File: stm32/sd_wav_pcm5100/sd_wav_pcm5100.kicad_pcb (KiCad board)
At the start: 2 copper layers, 39.7 x 50 mm, 79 parts, among them J1 BTN_1-4, J2 BTN_5-7, J3 BTN_8-11, P1 ST-LINK, P2 SPK_OUTL, P3 SPK_OUTR, P4 Supply, U1 STM32F410RBT6, U2 PCM5100, U3 PAM8403, U4 MX-503398-1892

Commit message: [sd_wav_pcm5100] updated board rev to 0.1
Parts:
- added REF**: 1pin, myfootprints:1pin, F.Cu at (72.8, 113.8)
- added REF**: 1pin, myfootprints:1pin, F.Cu at (73.8, 113.8)
- added REF**: 1pin, myfootprints:1pin, F.Cu at (72.8, 114.8)
- added REF**: 1pin, myfootprints:1pin, F.Cu at (73.8, 114.8)
- added REF**: 1pin, myfootprints:1pin, F.Cu at (73.8, 116.8)
- added REF**: 1pin, myfootprints:1pin, F.Cu at (72.8, 115.8)
- added REF**: 1pin, myfootprints:1pin, F.Cu at (73.8, 115.8)
- added REF**: 1pin, myfootprints:1pin, F.Cu at (72.8, 116.8)
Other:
- board text added: "Rev 0.1"
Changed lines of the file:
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@@
 (kicad_pcb (version 20160815) (host pcbnew no-vcs-found-7448~57~ubuntu16.04.1)
   (general
-    (links 146)
+    (links 154)
     (no_connects 0)
-    (area 56.39875 66.41875 100.59575 118.54175)
+    (area 59.074999 68.374999 98.875001 118.450018)
     (thickness 1.6)
-    (drawings 22)
-    (tracks 484)
+    (drawings 23)
+    (tracks 482)
     (zones 0)
-    (modules 79)
+    (modules 87)
     (nets 51)
   )
@@
     (add_net "Net-(R6-Pad2)")
   )
+  (module myfootprints:1pin (layer F.Cu)
+    (at 72.75 113.8)
+    (descr "module 1 pin (ou trou mecanique de percage)")
+    (tags DEV)
+    (fp_text reference REF** (at 0 -3.048) (layer F.SilkS) hide
+      (effects (font (size 0.6 0.6) (thickness 0.125)))
+    )
+    (fp_text value 1pin (at 0 2.794) (layer F.Fab) hide
+      (effects (font (size 0.6 0.6) (thickness 0.125)))
+    )
+    (pad "" thru_hole circle (at 0 0) (size 0.8 0.8) (drill 0.4) (layers *.Cu)
+      (net 1 GND) (zone_connect 2))
+  )
+  (module myfootprints:1pin (layer F.Cu)
+    (at 73.75 113.8)
+    (descr "module 1 pin (ou trou mecanique de percage)")
+    (tags DEV)
+    (fp_text reference REF** (at 0 -3.048) (layer F.SilkS) hide
+      (effects (font (size 0.6 0.6) (thickness 0.125)))
+    )
+    (fp_text value 1pin (at 0 2.794) (layer F.Fab) hide
+      (effects (font (size 0.6 0.6) (thickness 0.125)))
+    )
+    (pad "" thru_hole circle (at 0 0) (size 0.8 0.8) (drill 0.4) (layers *.Cu)
+      (net 1 GND) (zone_connect 2))
+  )
+  (module myfootprints:1pin (layer F.Cu)
+    (at 72.75 114.8)
+    (descr "module 1 pin (ou trou mecanique de percage)")
+    (tags DEV)
+    (fp_text reference REF** (at 0 -3.048) (layer F.SilkS) hide
+      (effects (font (size 0.6 0.6) (thickness 0.125)))
+    )
+    (fp_text value 1pin (at 0 2.794) (layer F.Fab) hide
+      (effects (font (size 0.6 0.6) (thickness 0.125)))
+    )
+    (pad "" thru_hole circle (at 0 0) (size 0.8 0.8) (drill 0.4) (layers *.Cu)
+      (net 1 GND) (zone_connect 2))
+  )
+  (module myfootprints:1pin (layer F.Cu)
+    (at 73.75 114.8)
+    (descr "module 1 pin (ou trou mecanique de percage)")
+    (tags DEV)
+    (fp_text reference REF** (at 0 -3.048) (layer F.SilkS) hide
+      (effects (font (size 0.6 0.6) (thickness 0.125)))
+    )
+    (fp_text value 1pin (at 0 2.794) (layer F.Fab) hide
+      (effects (font (size 0.6 0.6) (thickness 0.125)))
+    )
+    (pad "" thru_hole circle (at 0 0) (size 0.8 0.8) (drill 0.4) (layers *.Cu)
+      (net 1 GND) (zone_connect 2))
+  )
+  (module myfootprints:1pin (layer F.Cu)
+    (at 73.75 116.8)
+    (descr "module 1 pin (ou trou mecanique de percage)")
+    (tags DEV)
+    (fp_text reference REF** (at 0 -3.048) (layer F.SilkS) hide
+      (effects (font (size 0.6 0.6) (thickness 0.125)))
+    )
+    (fp_text value 1pin (at 0 2.794) (layer F.Fab) hide
+      (effects (font (size 0.6 0.6) (thickness 0.125)))
+    )
+    (pad "" thru_hole circle (at 0 0) (size 0.8 0.8) (drill 0.4) (layers *.Cu)
+      (net 1 GND) (zone_connect 2))
+  )
+  (module myfootprints:1pin (layer F.Cu)
+    (at 72.75 115.8)
+    (descr "module 1 pin (ou trou mecanique de percage)")
+    (tags DEV)
+    (fp_text reference REF** (at 0 -3.048) (layer F.SilkS) hide
+      (effects (font (size 0.6 0.6) (thickness 0.125)))
+    )
+    (fp_text value 1pin (at 0 2.794) (layer F.Fab) hide
+      (effects (font (size 0.6 0.6) (thickness 0.125)))
+    )
+    (pad "" thru_hole circle (at 0 0) (size 0.8 0.8) (drill 0.4) (layers *.Cu)
+      (net 1 GND) (zone_connect 2))
+  )
+  (module myfootprints:1pin (layer F.Cu)
+    (at 73.75 115.8)
+    (descr "module 1 pin (ou trou mecanique de percage)")
+    (tags DEV)
+    (fp_text reference REF** (at 0 -3.048) (layer F.SilkS) hide
+      (effects (font (size 0.6 0.6) (thickness 0.125)))
+    )
+    (fp_text value 1pin (at 0 2.794) (layer F.Fab) hide
+      (effects (font (size 0.6 0.6) (thickness 0.125)))
+    )
+    (pad "" thru_hole circle (at 0 0) (size 0.8 0.8) (drill 0.4) (layers *.Cu)
+      (net 1 GND) (zone_connect 2))
+  )
+  (module myfootprints:1pin (layer F.Cu)
+    (at 72.75 116.8)
+    (descr "module 1 pin (ou trou mecanique de percage)")
+    (tags DEV)
+    (fp_text reference REF** (at 0 -3.048) (layer F.SilkS) hide
+      (effects (font (size 0.6 0.6) (thickness 0.125)))
+    )
+    (fp_text value 1pin (at 0 2.794) (layer F.Fab) hide
+      (effects (font (size 0.6 0.6) (thickness 0.125)))
+    )
+    (pad "" thru_hole circle (at 0 0) (size 0.8 0.8) (drill 0.4) (layers *.Cu)
+      (net 1 GND) (zone_connect 2))
+  )
   (module myfootprints:TC-33X-2 (layer F.Cu)
     (at 80.44 103.26 90)
@@
       (effects (font (size 0.6 0.6) (thickness 0.125)))
     )
-    (fp_text value 47K (at 4.02278 -1.36 360) (layer F.SilkS)
+    (fp_text value 47K (at 4.02278 -1.36) (layer F.SilkS)
       (effects (font (size 0.6 0.6) (thickness 0.125)))
     )
@@
     )
   )
-  (gr_text "WAV Sound Module" (at 85.38 81.98 90) (layer B.SilkS)
+  (gr_text "Rev 0.1" (at 85.56 82.19 90) (layer B.SilkS)
+    (effects (font (size 0.8 0.8) (thickness 0.15)) (justify mirror))
+  )
+  (gr_text "WAV Sound Module" (at 84.17 82.17 90) (layer B.SilkS)
     (effects (font (size 0.8 0.8) (thickness 0.15)) (justify mirror))
   )
@@
   (segment (start 77.625 91.225) (end 77.45 91.05) (width 0.25) (layer F.Cu) (net 2) (status 30))
   (segment (start 77.45 91.05) (end 77.45 89.1) (width 0.25) (layer F.Cu) (net 2) (status 30))
+  (segment (start 71.95 89.1) (end 71.95 85.69) (width 0.25) (layer F.Cu) (net 3) (status 10))
+  (segment (start 71.95 85.69) (end 71.91 85.65) (width 0.25) (layer F.Cu) (net 3))
+  (segment (start 75.800002 85.65) (end 76.957004 85.65) (width 0.25) (layer F.Cu) (net 3))
+  (segment (start 76.957004 85.65) (end 78.45 87.142996) (width 0.25) (layer F.Cu) (net 3))
+  (segment (start 78.45 87.142996) (end 78.45 88.725) (width 0.25) (layer F.Cu) (net 3) (status 20))
+  (segment (start 78.45 88.725) (end 78.45 89.1) (width 0.25) (layer F.Cu) (net 3) (status 30))
   (segment (start 73.54 108.35) (end 73.54 111.35) (width 0.45) (layer B.Cu) (net 3))
   (segment (start 73.54 111.35) (end 76.95 111.35) (width 0.45) (layer B.Cu) (net 3))
@@
   (segment (start 78.362998 79.65) (end 75.800002 82.212996) (width 0.25) (layer F.Cu) (net 3))
   (segment (start 75.800002 82.212996) (end 75.800002 85.65) (width 0.25) (layer F.Cu) (net 3))
-  (segment (start 78.825 88.35) (end 78.45 88.725) (width 0.25) (layer F.Cu) (net 3) (status 20))
-  (segment (start 78.825 87.517996) (end 78.825 88.35) (width 0.25) (layer F.Cu) (net 3))
-  (segment (start 76.957004 85.65) (end 78.825 87.517996) (width 0.25) (layer F.Cu) (net 3))
-  (segment (start 75.800002 85.65) (end 76.957004 85.65) (width 0.25) (layer F.Cu) (net 3))
-  (segment (start 78.45 88.725) (end 78.45 89.1) (width 0.25) (layer F.Cu) (net 3) (status 30))
   (segment (start 68.795 93.28) (end 68.55 93.525) (width 0.25) (layer F.Cu) (net 3) (status 30))
-  (segment (start 71.91 88.31) (end 71.91 85.65) (width 0.25) (layer F.Cu) (net 3))
   (segment (start 69 85.65) (end 71.91 85.65) (width 0.25) (layer F.Cu) (net 3) (status 10))
   (segment (start 71.91 85.65) (end 75.800002 85.65) (width 0.25) (layer F.Cu) (net 3))
-  (segment (start 71.95 89.1) (end 71.95 88.35) (width 0.25) (layer F.Cu) (net 3) (status 10))
-  (segment (start 71.95 88.35) (end 71.91 88.31) (width 0.25) (layer F.Cu) (net 3))
   (segment (start 68.35 109.275) (end 68.35 110.22) (width 0.45) (layer F.Cu) (net 3) (status 10))
   (segment (start 66.39 110.42) (end 62.725 114.085) (width 0.45) (layer F.Cu) (net 3) (status 20))
@@
   (segment (start 72.95 94.277878) (end 72.95 89.1) (width 0.25) (layer F.Cu) (net 47) (status 20))
   (segment (start 73.39 94.717878) (end 72.95 94.277878) (width 0.25) (layer F.Cu) (net 47))
-  (segment (start 75.23 90.052273) (end 72.68501 87.507283) (width 0.25) (layer B.Cu) (net 48))
-  (segment (start 75.23 95.24) (end 75.23 90.052273) (width 0.25) (layer B.Cu) (net 48))
-  (segment (start 72.45 89.1) (end 72.45 87.742293) (width 0.25) (layer F.Cu) (net 48) (status 10))
-  (segment (start 72.45 87.742293) (end 72.68501 87.507283) (width 0.25) (layer F.Cu) (net 48))
-  (via (at 72.68501 87.507283) (size 0.8) (drill 0.4) (layers F.Cu B.Cu) (net 48))
+  (segment (start 72.72501 92.73501) (end 72.72501 87.507283) (width 0.25) (layer B.Cu) (net 48))
+  (segment (start 72.45 87.782293) (end 72.72501 87.507283) (width 0.25) (layer F.Cu) (net 48))
+  (segment (start 75.23 95.24) (end 72.72501 92.73501) (width 0.25) (layer B.Cu) (net 48))
+  (segment (start 72.45 89.1) (end 72.45 87.782293) (width 0.25) (layer F.Cu) (net 48) (status 10))
+  (via (at 72.72501 87.507283) (size 0.8) (drill 0.4) (layers F.Cu B.Cu) (net 48))
   (segment (start 77.47 96.53) (end 76.495 96.53) (width 0.25) (layer F.Cu) (net 48) (status 10))
   (segment (start 76.495 96.53) (end 75.23 95.265) (width 0.25) (layer F.Cu) (net 48))

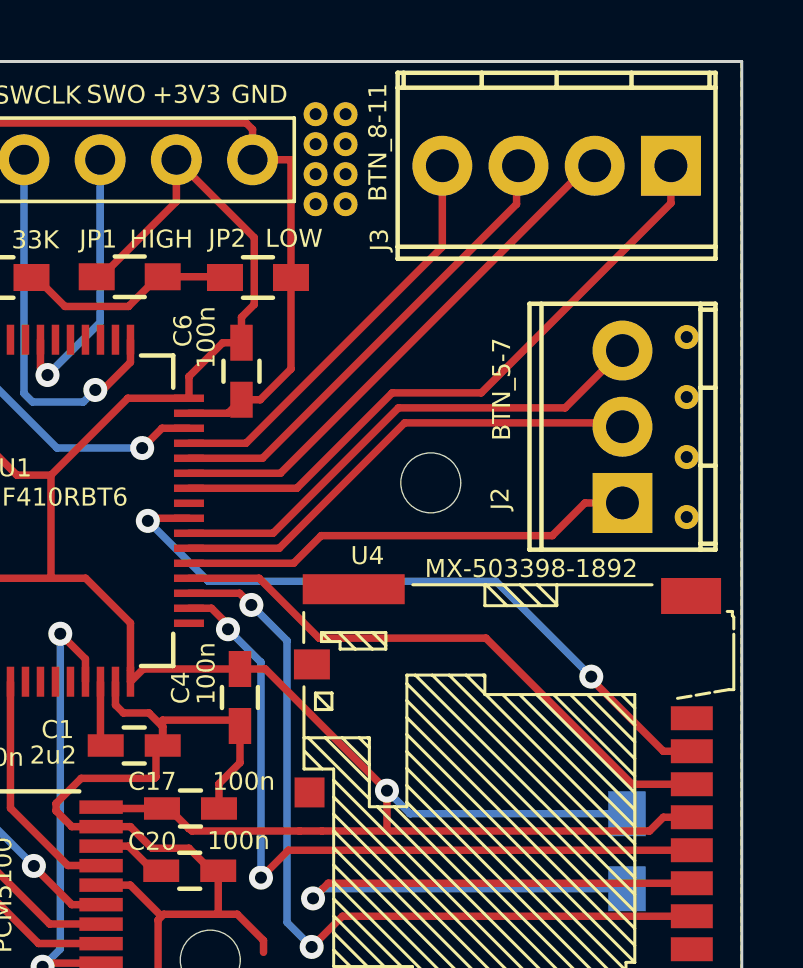
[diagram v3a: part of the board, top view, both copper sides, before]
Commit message: [sd_wav_pcm5100] more stitches
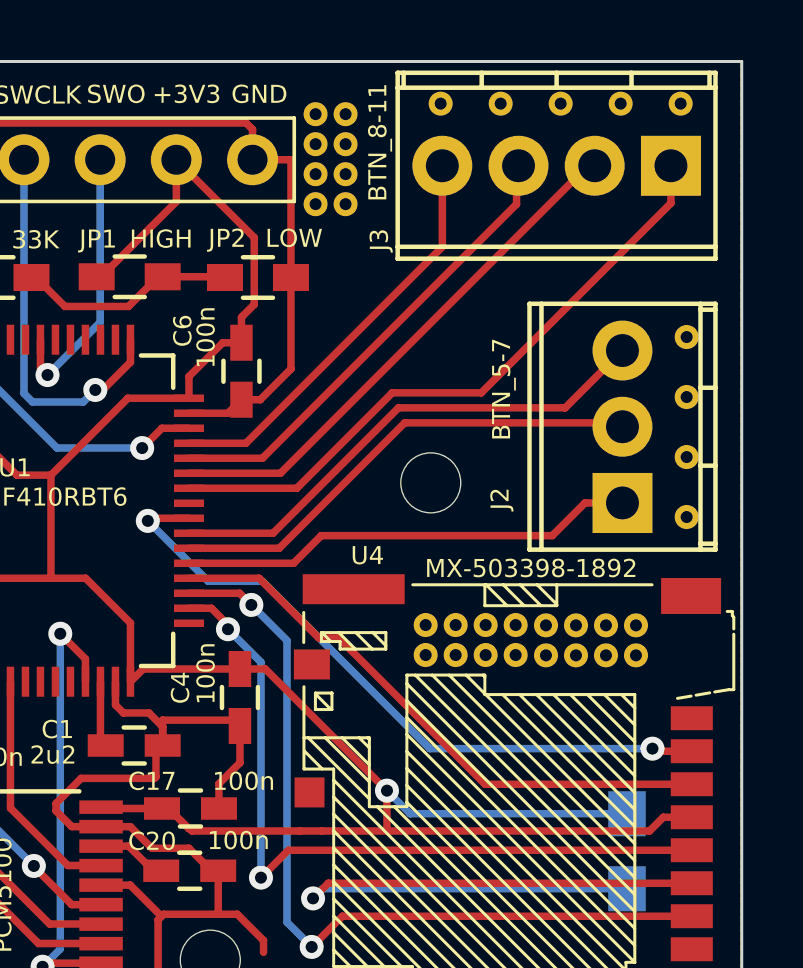
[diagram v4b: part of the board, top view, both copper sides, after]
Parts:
- added REF**: 1pin, myfootprints:1pin, F.Cu at (92.3, 87.2)
- added REF**: 1pin, myfootprints:1pin, F.Cu at (90.3, 87.2)
- added REF**: 1pin, myfootprints:1pin, F.Cu at (90.3, 88.2)
- added REF**: 1pin, myfootprints:1pin, F.Cu at (91.3, 87.2)
- added REF**: 1pin, myfootprints:1pin, F.Cu at (91.3, 88.2)
- added REF**: 1pin, myfootprints:1pin, F.Cu at (88.3, 87.2)
- added REF**: 1pin, myfootprints:1pin, F.Cu at (88.3, 88.2)
- added REF**: 1pin, myfootprints:1pin, F.Cu at (89.3, 87.2)
- added REF**: 1pin, myfootprints:1pin, F.Cu at (94.8, 69.8)
- added REF**: 1pin, myfootprints:1pin, F.Cu at (90.8, 69.8)
- added REF**: 1pin, myfootprints:1pin, F.Cu at (92.8, 69.8)
- added REF**: 1pin, myfootprints:1pin, F.Cu at (93.3, 88.2)
- added REF**: 1pin, myfootprints:1pin, F.Cu at (96.8, 69.8)
- added REF**: 1pin, myfootprints:1pin, F.Cu at (88.8, 69.8)
- added REF**: 1pin, myfootprints:1pin, F.Cu at (93.3, 87.2)
- added REF**: 1pin, myfootprints:1pin, F.Cu at (94.3, 88.2)
- added REF**: 1pin, myfootprints:1pin, F.Cu at (94.3, 87.2)
- added REF**: 1pin, myfootprints:1pin, F.Cu at (95.3, 87.2)
- added REF**: 1pin, myfootprints:1pin, F.Cu at (92.3, 88.2)
- added REF**: 1pin, myfootprints:1pin, F.Cu at (95.3, 88.2)
- added REF**: 1pin, myfootprints:1pin, F.Cu at (89.3, 88.2)
